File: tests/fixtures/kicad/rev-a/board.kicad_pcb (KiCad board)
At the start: 2 copper layers, 2 parts, among them U1 LDO

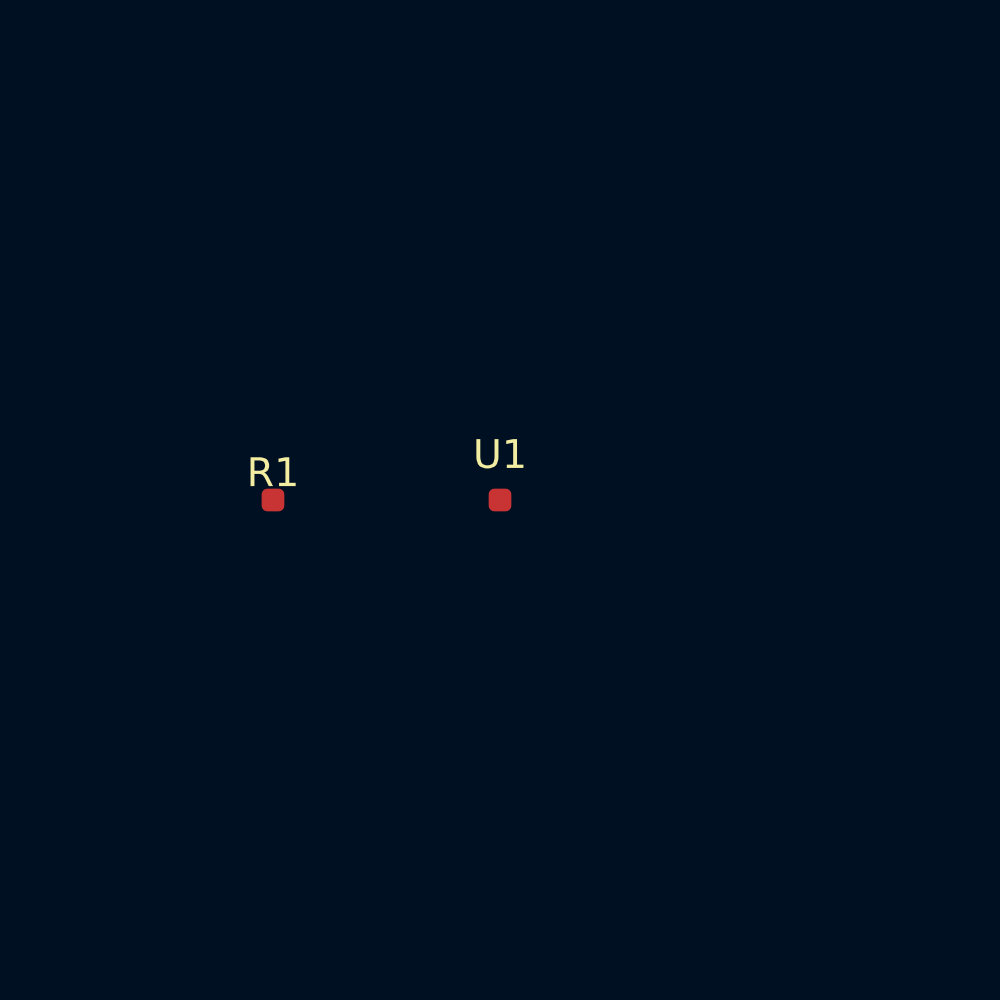
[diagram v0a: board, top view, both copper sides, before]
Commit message: feat: add PCB DFM DFA DFT precheck
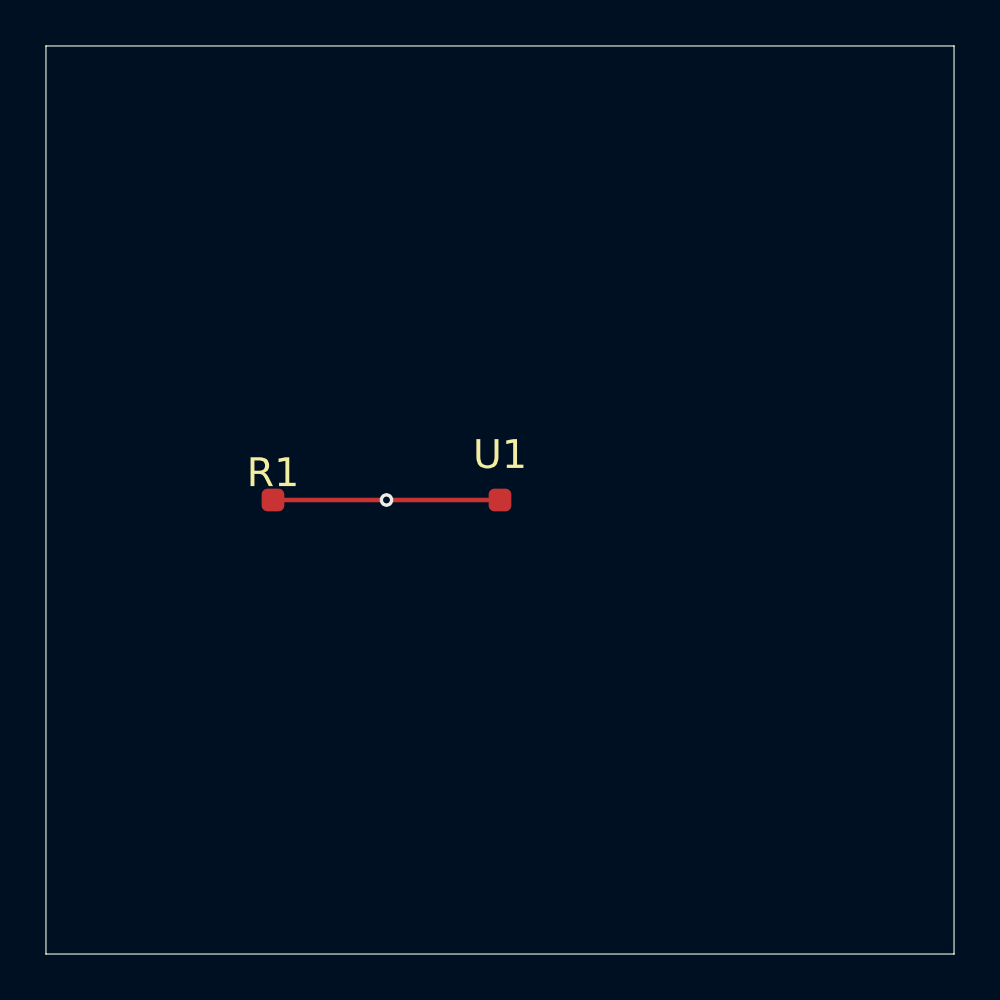
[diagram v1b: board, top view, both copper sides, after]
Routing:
- net VCC_3V3: track 0.00 -> 10.0 mm, vias 0 -> 1
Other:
- board outline added: 40 x 40 mm
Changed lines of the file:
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@@
   (net 1 "GND")
   (net 2 "VCC_3V3")
+  (gr_line (start 0 0) (end 40 0) (stroke (width 0.05) (type default)) (layer "Edge.Cuts"))
+  (gr_line (start 40 0) (end 40 40) (stroke (width 0.05) (type default)) (layer "Edge.Cuts"))
+  (gr_line (start 40 40) (end 0 40) (stroke (width 0.05) (type default)) (layer "Edge.Cuts"))
+  (gr_line (start 0 40) (end 0 0) (stroke (width 0.05) (type default)) (layer "Edge.Cuts"))
+  (segment (start 10 20) (end 20 20) (width 0.2) (layer "F.Cu") (net 2))
+  (via (at 15 20) (size 0.6) (drill 0.3) (layers "F.Cu" "B.Cu") (net 2))
   (footprint "Resistor_SMD:R_0603_1608Metric"
     (layer "F.Cu")
